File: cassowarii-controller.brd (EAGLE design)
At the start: 34.3 x 26.7 mm, 21 parts, among them J1 2-PIN_2MM-H, J2 2-PIN_2MM-H, J3 AVR_SPI_PROG_3X2PTH, J4 Power, U1 ATTiny85, U2 AZ1117IH

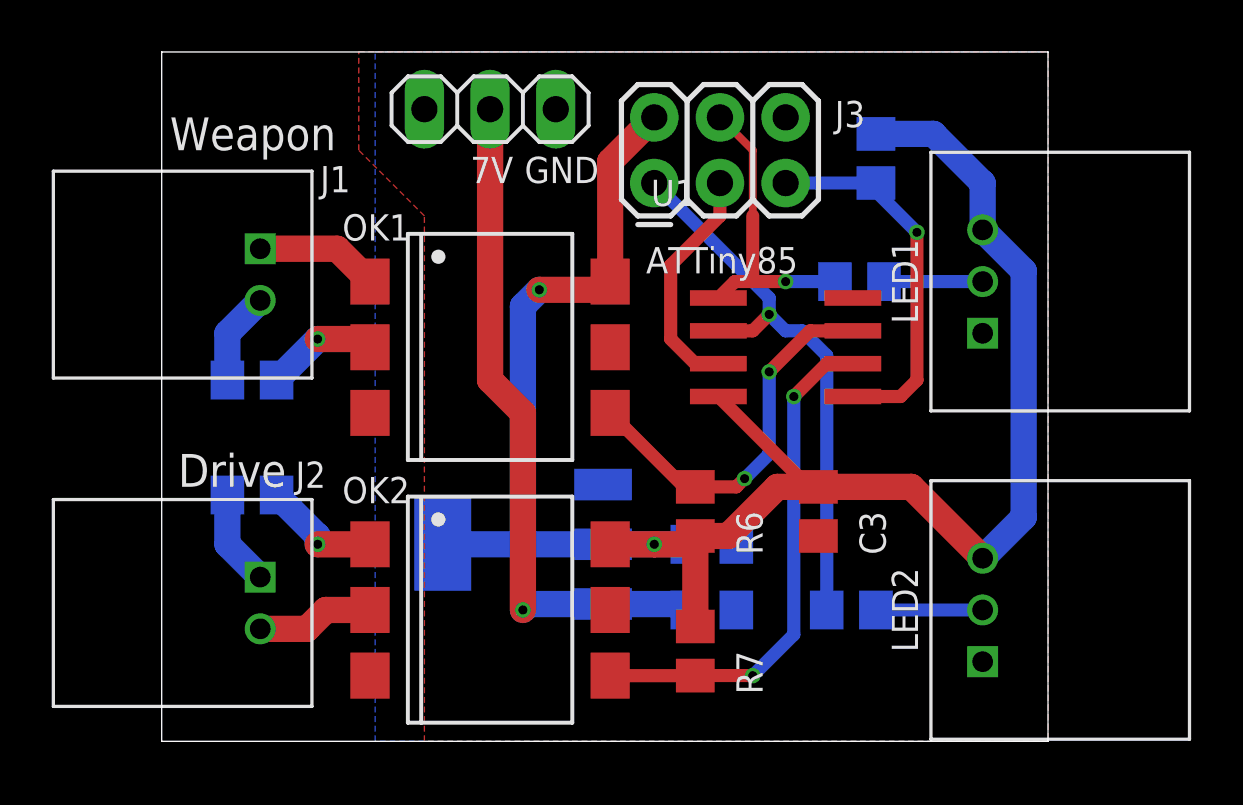
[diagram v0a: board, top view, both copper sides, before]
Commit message: Add spots for through hole power resistors
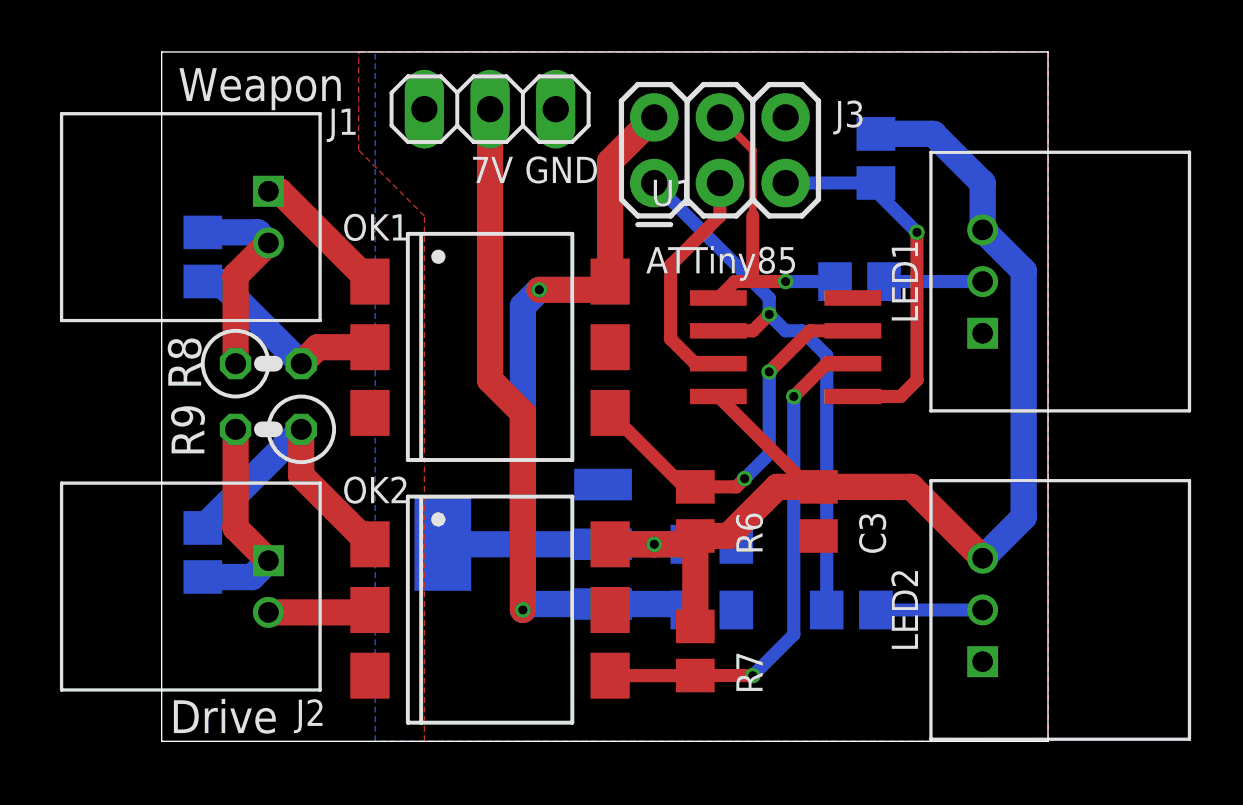
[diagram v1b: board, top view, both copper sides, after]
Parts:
- added R8: 3.9k, resistor:0207/2V
- added R9: 1.5k, resistor:0207/2V
- R2: value 3.9k -> NP
- R3: value 1.5k -> NP
- moved R2 5.13 mm to (1.59, 18.7), turned to 90 degrees
- moved R3 2.93 mm to (1.59, 7.30), turned to 90 degrees
- moved J1 2.25 mm to (4.13, 21.3)
- moved J2 0.71 mm to (4.13, 6.99)
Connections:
- net N$10: now also R9.1
- net N$3: now also R9.2
- net N$4: now also R2.2, R8.1; no longer R2.1
- net N$5: now also R2.1, R8.2; no longer R2.2
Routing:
- net N$10: track 4.59 -> 10.9 mm, vias 1 -> 0
- net N$3: track 3.70 -> 8.41 mm
- net N$4: track 3.61 -> 7.90 mm
- net N$5: track 4.40 -> 8.50 mm, vias 1 -> 0
- net N$7: track 4.77 -> 5.37 mm
- net N$6: track 4.55 -> 3.97 mm

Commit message: Remove regulator
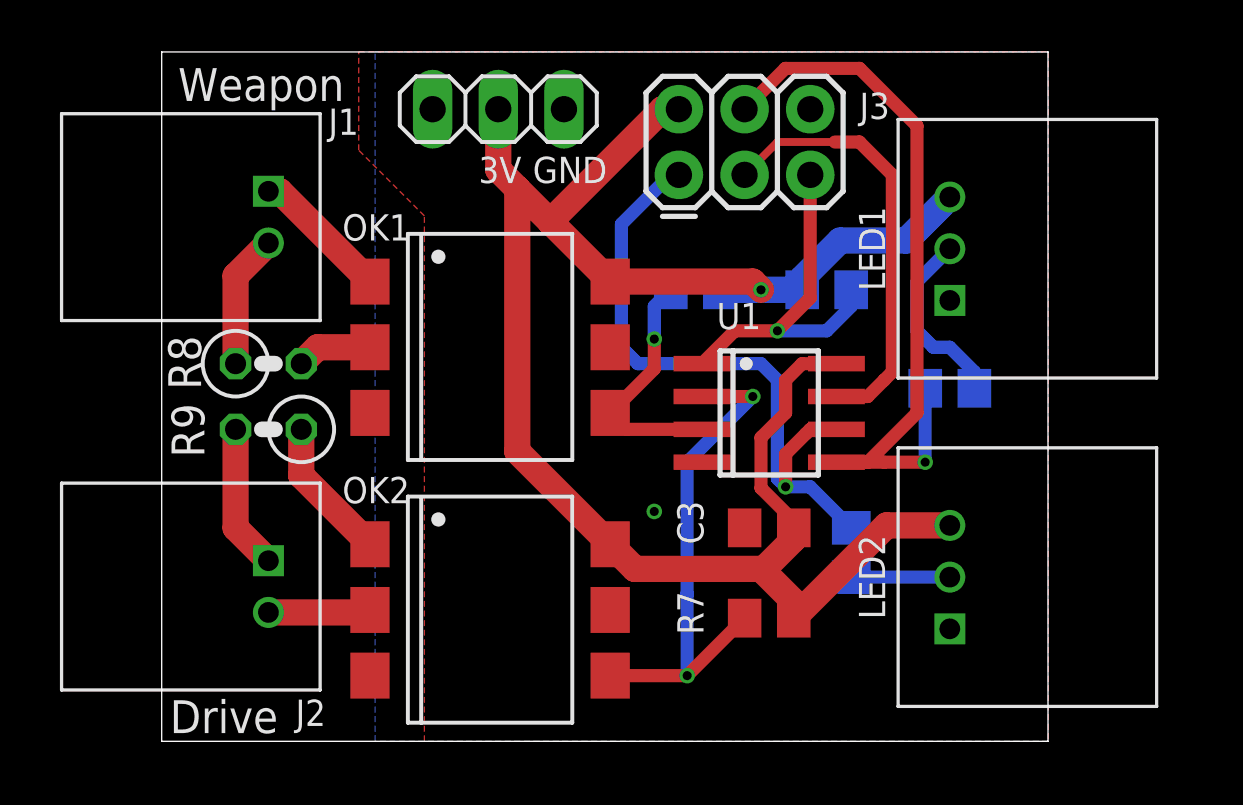
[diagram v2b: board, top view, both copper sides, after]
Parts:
- removed C1, C2: 22uF, resistor:C0805
- removed R2, R3: NP, resistor:R0805
- removed U2: AZ1117IH, JoshCustom:SOT223
- moved R6 8.57 mm to (20.6, 17.5), flipped to the bottom, turned to 180 degrees
- moved R1 5.43 mm to (25.7, 17.5), turned to 0 degrees
- moved R4 5.41 mm to (30.5, 13.7)
- moved U$1 4.02 mm to (14.0, 10.2)
- moved R7 3.13 mm to (23.5, 4.76), turned to 0 degrees
- moved U1 2.62 mm to (23.5, 12.7), turned to 270 degrees
- moved R5 2.22 mm to (26.7, 7.30), turned to 270 degrees
- moved C3 2.01 mm to (23.5, 8.26), turned to 180 degrees
- moved LED1 1.80 mm to (30.5, 19.1)
- moved LED2 1.80 mm to (30.5, 6.35)
- moved J3 1.00 mm to (20.0, 21.9)
- moved J4 0.32 mm to (13.0, 24.4)
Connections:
- removed net VIN: C1.1, J4.2, U2.3
- net GND: no longer C1.2, C2.2, U2.1
- net N$10: no longer R3.2
- net N$3: no longer R3.1
- net N$4: no longer R2.2
- net N$5: no longer R2.1
- net VCC: now also J4.2; no longer C2.1, U2.2, U2.4
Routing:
- net VIN: track 26.4 -> 0.00 mm, vias 1 -> 0
- net LED2: track 11.6 -> 28.3 mm
- net PB2: track 9.06 -> 16.9 mm
- net N$5: track 8.50 -> 2.92 mm
- net N$10: track 10.9 -> 5.55 mm
- net PB4: track 14.9 -> 9.55 mm, vias 2 -> 1
- net LED1: track 21.9 -> 25.4 mm
- net N$1: track 3.81 -> 7.22 mm
- net N$3: track 8.41 -> 5.61 mm
- net N$4: track 7.90 -> 5.19 mm
- net VCC: track 75.5 -> 74.3 mm, vias 2 -> 1
- net RESET: track 14.5 -> 13.9 mm
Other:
- board text added: "3V"
- board text removed: "7V"
- board text removed: "ATTiny85"
